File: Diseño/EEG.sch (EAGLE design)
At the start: 29 parts

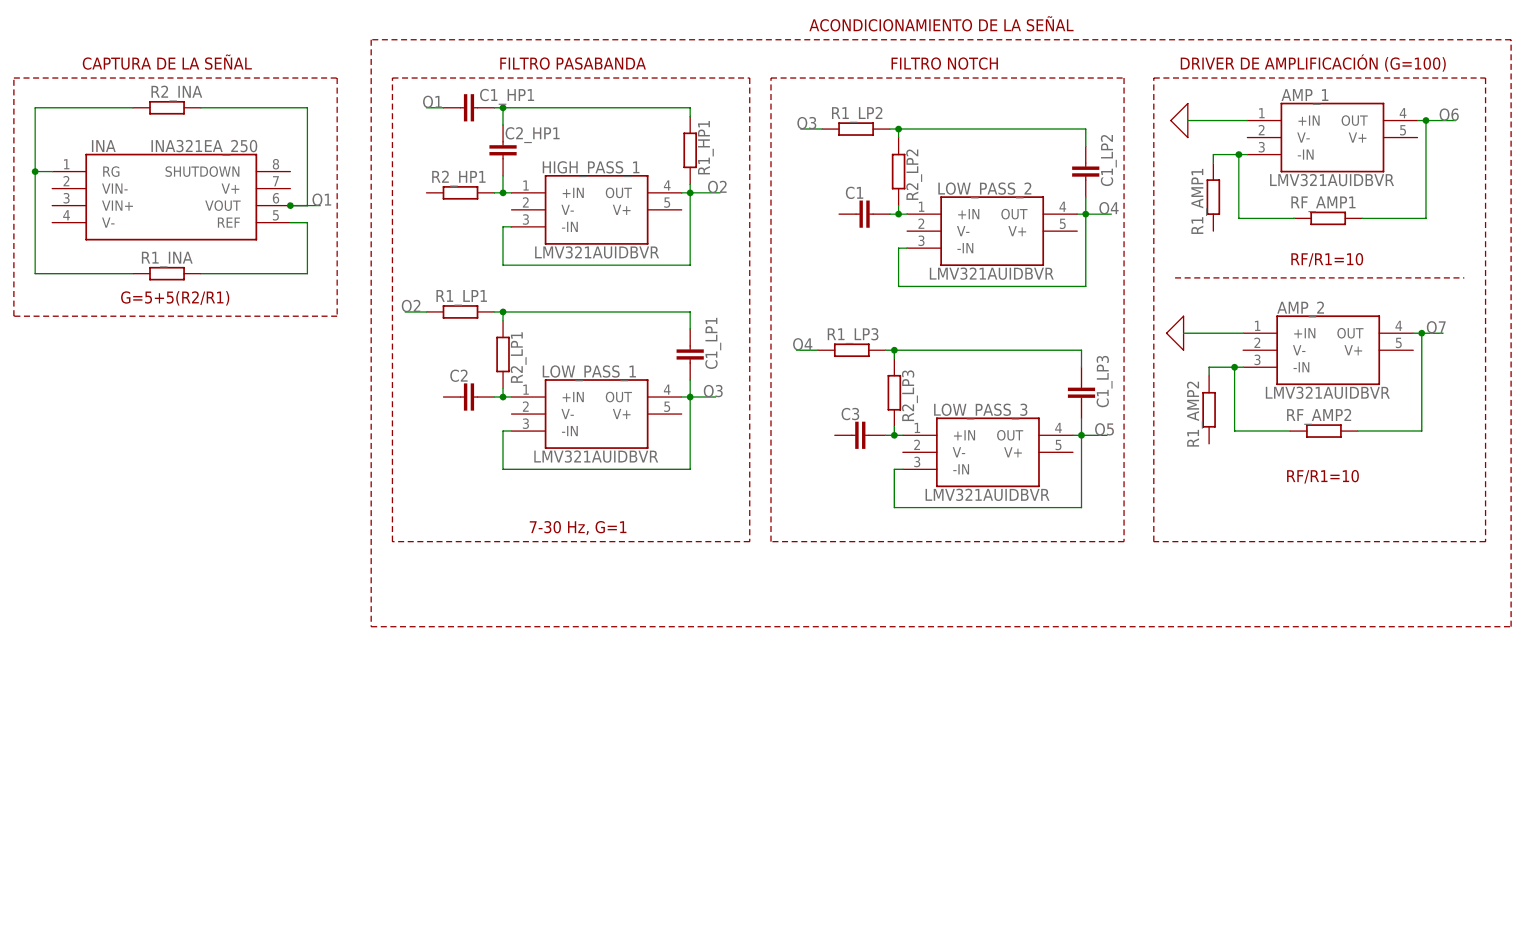
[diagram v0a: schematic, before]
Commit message: Se reemplazó el INA y se agregó la ESP32 (faltan por configurar)
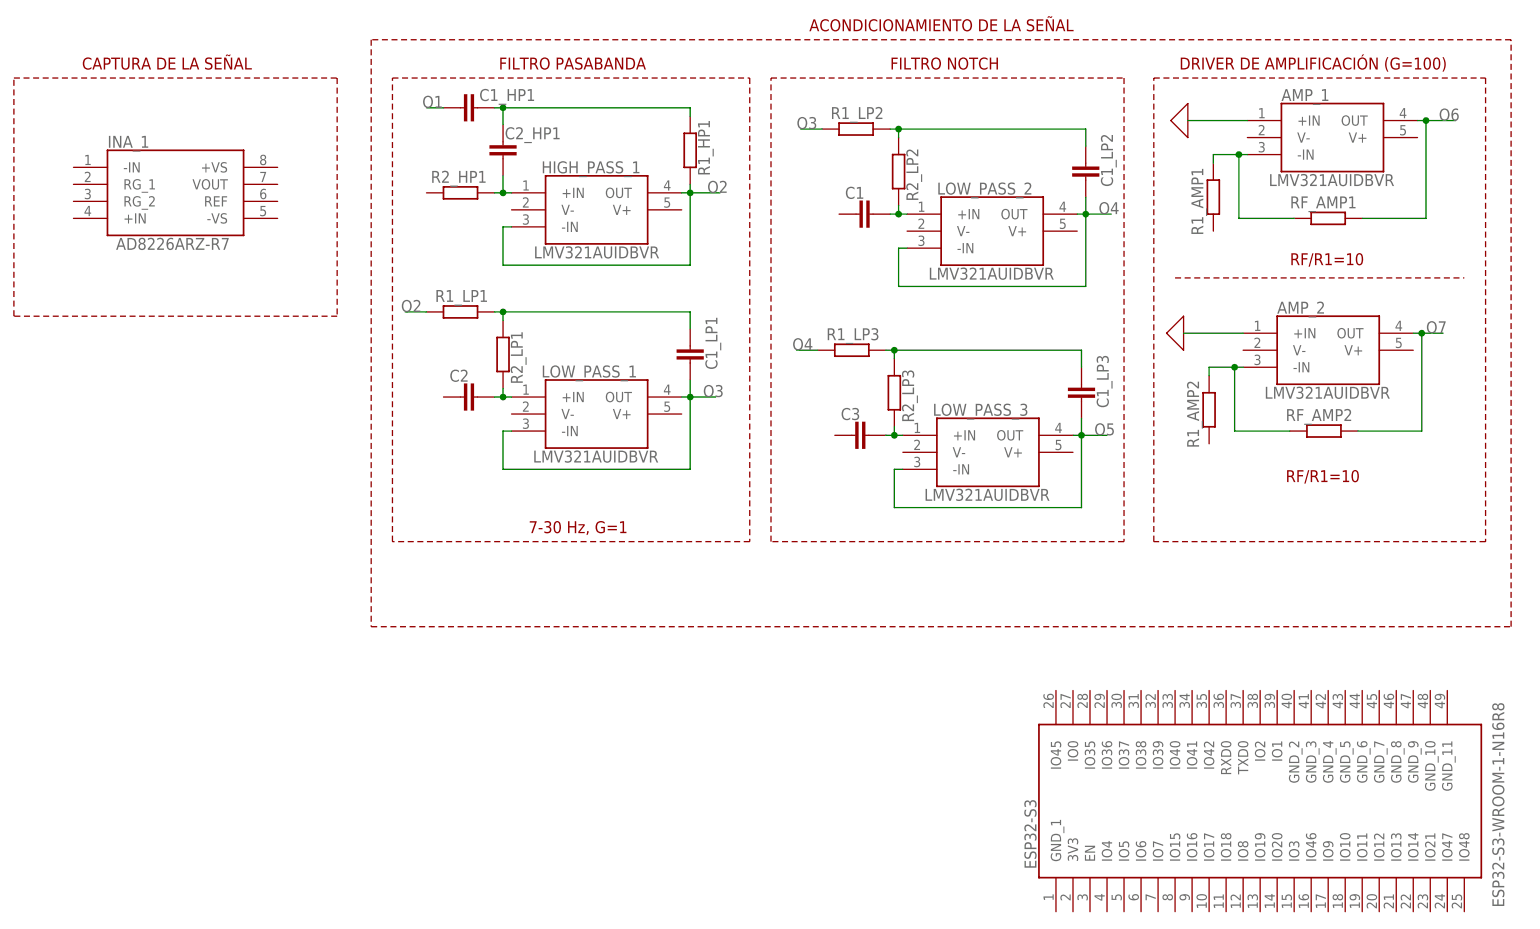
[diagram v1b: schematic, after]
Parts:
- removed INA: INA321EA_250, INA321EA_250:INA321EA_250
- removed R1_INA, R2_INA: (no value), rcl:R-EU_R0805
- added ESP32-S3: ESP32-S3-WROOM-1-N16R8, ESP32-S3-WROOM-1-N16R8:ESP32-S3-WROOM-1-N16R8
- added INA_1: AD8226ARZ-R7, AD8226ARZ-R7:AD8226ARZ-R7
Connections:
- removed net N$1: INA.RG, R1_INA.1, R2_INA.1
- removed net N$2: INA.REF, R1_INA.2
- net O1: no longer INA.VOUT, R2_INA.2
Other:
- note removed: "G=5+5(R2/R1)"
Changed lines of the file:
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@@
 <parts>
 <part name="FRAME1" library="frames" library_urn="urn:adsk.eagle:library:229" deviceset="LETTER_L" device=""/>
-<part name="INA" library="INA321EA_250" deviceset="INA321EA_250" device=""/>
-<part name="R1_INA" library="rcl" library_urn="urn:adsk.eagle:library:334" deviceset="R-EU_" device="R0805" package3d_urn="urn:adsk.eagle:package:23553/2"/>
-<part name="R2_INA" library="rcl" library_urn="urn:adsk.eagle:library:334" deviceset="R-EU_" device="R0805" package3d_urn="urn:adsk.eagle:package:23553/2"/>
 <part name="HIGH_PASS_1" library="LMV321AUIDBVR" deviceset="LMV321AUIDBVR" device=""/>
 <part name="LOW_PASS_1" library="LMV321AUIDBVR" deviceset="LMV321AUIDBVR" device=""/>
@@
 <part name="R2_LP3" library="rcl" library_urn="urn:adsk.eagle:library:334" deviceset="R-EU_" device="R0805" package3d_urn="urn:adsk.eagle:package:23553/2"/>
 <part name="C3" library="rcl" library_urn="urn:adsk.eagle:library:334" deviceset="C-EU" device="C0805" package3d_urn="urn:adsk.eagle:package:23617/2"/>
+<part name="INA_1" library="AD8226ARZ-R7" deviceset="AD8226ARZ-R7" device=""/>
+<part name="ESP32-S3" library="ESP32-S3-WROOM-1-N16R8" deviceset="ESP32-S3-WROOM-1-N16R8" device=""/>
 </parts>
 <sheets>
@@
 <wire x1="67.945" y1="133.35" x2="19.685" y2="133.35" width="0.1524" layer="94" style="shortdash"/>
 <wire x1="19.685" y1="133.35" x2="19.685" y2="168.91" width="0.1524" layer="94" style="shortdash"/>
-<text x="35.56" y="135.255" size="1.778" layer="94">G=5+5(R2/R1)</text>
 <text x="29.845" y="170.18" size="1.778" layer="94">CAPTURA DE LA SEÑAL</text>
 <wire x1="73.025" y1="174.625" x2="73.025" y2="86.995" width="0.1524" layer="94" style="shortdash"/>
@@
 <attribute name="SHEET" x="233.68" y="1.27" size="2.54" layer="94"/>
 <attribute name="DRAWING_NAME" x="165.1" y="19.05" size="2.54" layer="94"/>
-</instance>
-<instance part="INA" gate="G$1" x="25.4" y="154.94" smashed="yes">
-<attribute name="NAME" x="31.115" y="158.75" size="1.778" layer="95" align="center-left"/>
-<attribute name="VALUE" x="40.005" y="158.75" size="1.778" layer="96" align="center-left"/>
-</instance>
-<instance part="R1_INA" gate="G$1" x="42.545" y="139.7" smashed="yes">
-<attribute name="NAME" x="38.57625" y="141.1986" size="1.778" layer="95"/>
-<attribute name="VALUE" x="38.735" y="136.398" size="1.778" layer="96"/>
-</instance>
-<instance part="R2_INA" gate="G$1" x="42.545" y="164.465" smashed="yes">
-<attribute name="NAME" x="40.005" y="165.9636" size="1.778" layer="95"/>
-<attribute name="VALUE" x="38.735" y="161.163" size="1.778" layer="96"/>
 </instance>
 <instance part="HIGH_PASS_1" gate="G$1" x="93.98" y="151.765" smashed="yes">
@@
 <attribute name="VALUE" x="142.621" y="114.046" size="1.778" layer="96" rot="R270"/>
 </instance>
+<instance part="INA_1" gate="G$1" x="28.575" y="155.575" smashed="yes">
+<attribute name="NAME" x="33.655" y="159.385" size="1.778" layer="95" align="center-left"/>
+<attribute name="VALUE" x="34.925" y="144.145" size="1.778" layer="96" align="center-left"/>
+</instance>
+<instance part="ESP32-S3" gate="G$1" x="175.26" y="44.45" smashed="yes" rot="R90">
+<attribute name="NAME" x="171.45" y="50.8" size="1.778" layer="95" rot="R90" align="center-left"/>
+<attribute name="VALUE" x="241.3" y="45.085" size="1.778" layer="96" rot="R90" align="center-left"/>
+</instance>
 </instances>
 <busses>
 </busses>
 <nets>
-<net name="N$2" class="0">
-<segment>
-<pinref part="INA" gate="G$1" pin="REF"/>
-<wire x1="60.96" y1="147.32" x2="63.5" y2="147.32" width="0.1524" layer="91"/>
-<wire x1="63.5" y1="147.32" x2="63.5" y2="139.7" width="0.1524" layer="91"/>
-<pinref part="R1_INA" gate="G$1" pin="2"/>
-<wire x1="63.5" y1="139.7" x2="47.625" y2="139.7" width="0.1524" layer="91"/>
-</segment>
-</net>
 <net name="O1" class="0">
-<segment>
-<pinref part="INA" gate="G$1" pin="VOUT"/>
-<wire x1="60.96" y1="149.86" x2="63.5" y2="149.86" width="0.1524" layer="91"/>
-<pinref part="R2_INA" gate="G$1" pin="2"/>
-<wire x1="63.5" y1="149.86" x2="63.5" y2="164.465" width="0.1524" layer="91"/>
-<wire x1="63.5" y1="164.465" x2="47.625" y2="164.465" width="0.1524" layer="91"/>
-<wire x1="60.96" y1="149.86" x2="65.405" y2="149.86" width="0.1524" layer="91"/>
-<junction x="60.96" y="149.86"/>
-<label x="64.135" y="149.86" size="1.778" layer="95"/>
-</segment>
 <segment>
 <pinref part="C1_HP1" gate="G$1" pin="1"/>
@@
 </segment>
 </net>
-<net name="N$1" class="0">
-<segment>
-<pinref part="R1_INA" gate="G$1" pin="1"/>
-<wire x1="37.465" y1="139.7" x2="22.86" y2="139.7" width="0.1524" layer="91"/>
-<pinref part="INA" gate="G$1" pin="RG"/>
-<wire x1="22.86" y1="139.7" x2="22.86" y2="154.94" width="0.1524" layer="91"/>
-<wire x1="22.86" y1="154.94" x2="25.4" y2="154.94" width="0.1524" layer="91"/>
-<pinref part="R2_INA" gate="G$1" pin="1"/>
-<wire x1="37.465" y1="164.465" x2="22.86" y2="164.465" width="0.1524" layer="91"/>
-<wire x1="22.86" y1="164.465" x2="22.86" y2="154.94" width="0.1524" layer="91"/>
-<junction x="22.86" y="154.94"/>
-</segment>
-</net>

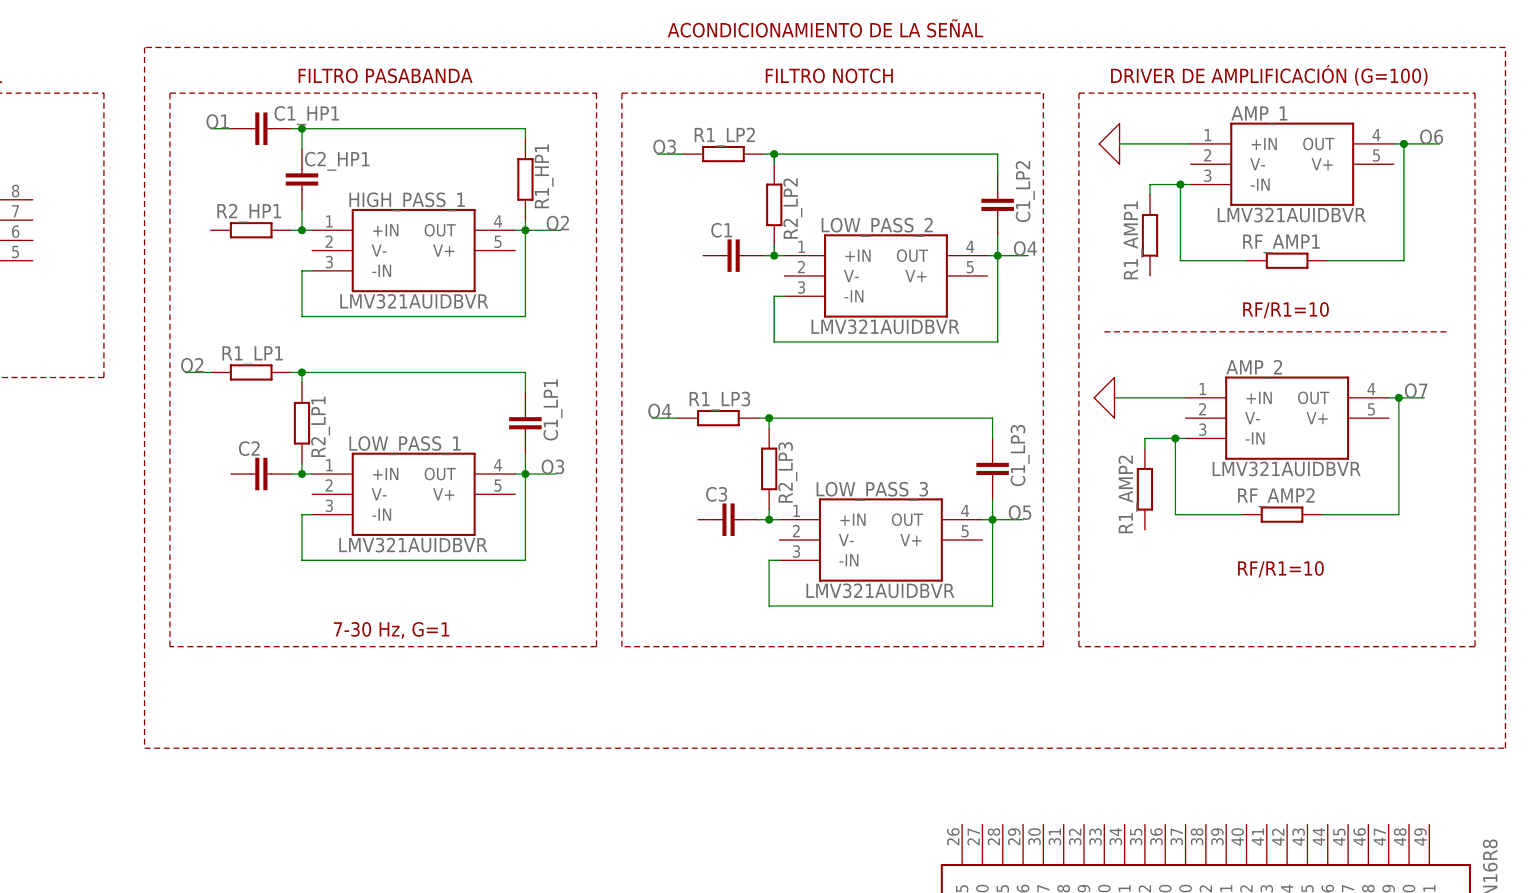
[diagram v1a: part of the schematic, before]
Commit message: se quita el filtro Notch ; a la espera de corregir valores de salidas v2
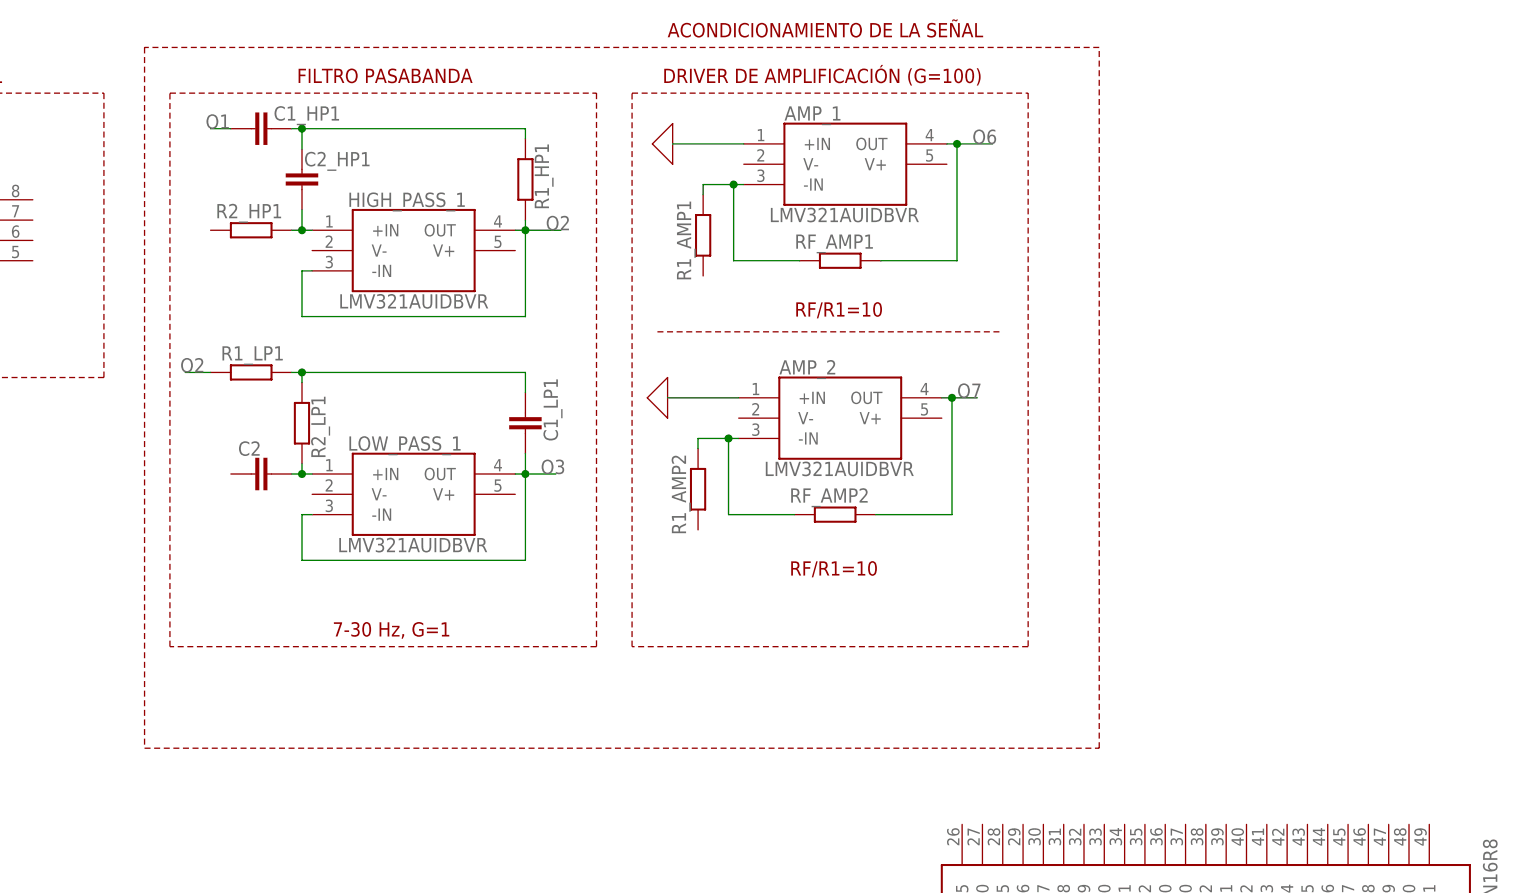
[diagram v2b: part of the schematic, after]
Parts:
- removed C1, C1_LP2, C1_LP3, C3: (no value), rcl:C-EUC0805
- removed LOW_PASS_2, LOW_PASS_3: LMV321AUIDBVR, LMV321AUIDBVR:LMV321AUIDBVR
- removed R1_LP2, R1_LP3, R2_LP2, R2_LP3: (no value), rcl:R-EU_R0805
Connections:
- removed net N$11: C1_LP2.1, R1_LP2.2, R2_LP2.1
- removed net N$12: C1.1, LOW_PASS_2.+IN, R2_LP2.2
- removed net N$13: C1_LP3.1, R1_LP3.2, R2_LP3.1
- removed net N$14: C3.1, LOW_PASS_3.+IN, R2_LP3.2
- removed net O4: C1_LP2.2, LOW_PASS_2.-IN, LOW_PASS_2.OUT, R1_LP3.1
- removed net O5: C1_LP3.2, LOW_PASS_3.-IN, LOW_PASS_3.OUT
- net O3: no longer R1_LP2.1
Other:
- note removed: "FILTRO NOTCH"
- moved on the sheet: AMP_1, AMP_2, R1_AMP1, R1_AMP2, RF_AMP1, RF_AMP2
